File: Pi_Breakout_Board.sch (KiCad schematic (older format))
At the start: 74 parts, among them J1 Raspberry_Pi_2_3, J2 Conn_02x04_Odd_Even heater he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, J3 Conn_02x08_Odd_Even thermisto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, J4 Screw_Terminal_01x02, J5 Conn_01x08_Male, J6 Conn_01x08_Male, J7 Conn_01x02_Female, J8 Conn_01x03_Male, Q1 Q_NMOS_GDSD, Q2 Q_NMOS_GDSD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

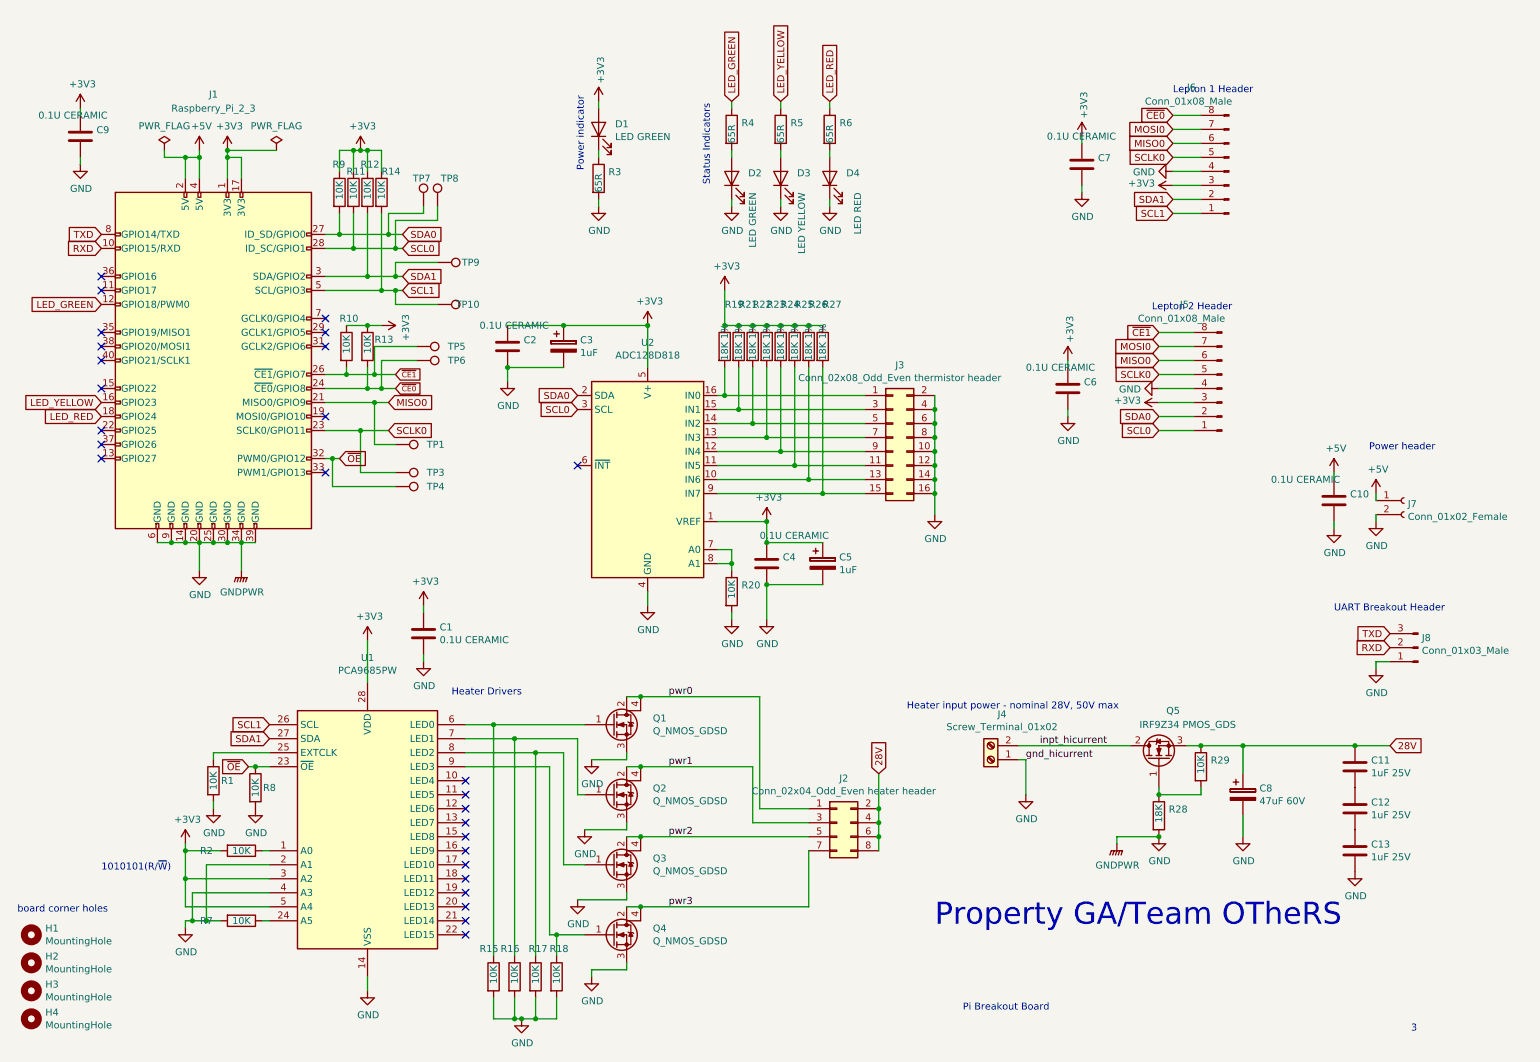
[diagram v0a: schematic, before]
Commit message: Routing updates + double checks. Silkscreen
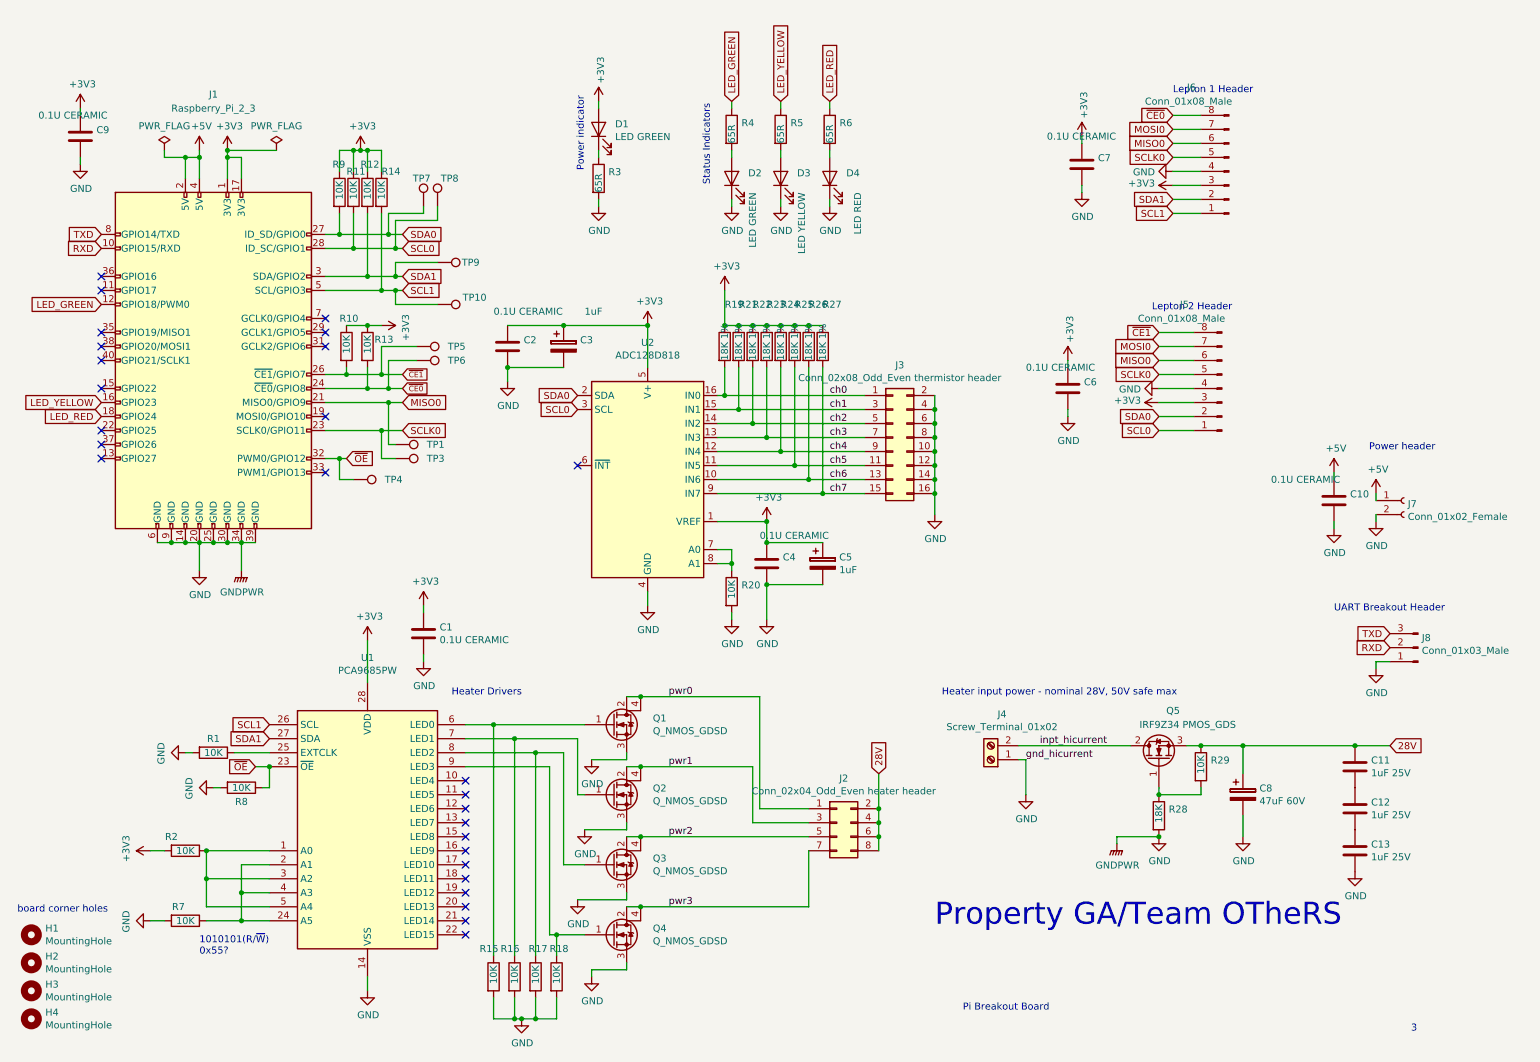
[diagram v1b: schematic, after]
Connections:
- net +3V3: no longer U1.3 (A2), U1.5 (A4)
- net GND: no longer U1.2 (A1), U1.4 (A3)
- net at R7.1, U1.24 (A5): now also U1.2 (A1), U1.4 (A3)
- net at R2.1, U1.1 (A0): now also U1.3 (A2), U1.5 (A4)
- net ch6: now reaches J3.13 (Pin_13), R26.2, U2.10 (IN6)
- net ch5: now reaches J3.11 (Pin_11), R25.2, U2.11 (IN5)
- net ch4: now reaches J3.9 (Pin_9), R24.2, U2.12 (IN4)
- net ch3: now reaches J3.7 (Pin_7), R23.2, U2.13 (IN3)
- net ch2: now reaches J3.5 (Pin_5), R22.2, U2.14 (IN2)
- net ch1: now reaches J3.3 (Pin_3), R21.2, U2.15 (IN1)
- net ch0: now reaches J3.1 (Pin_1), R19.2, U2.16 (IN0)
- net ch7: now reaches J3.15 (Pin_15), R27.2, U2.9 (IN7)
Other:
- note added: "1010101(R/~W)\n0x55?"
- note added: "Heater input power - nominal 28V, 50V safe max"
- note removed: "1010101(R/~W)"
- note removed: "Heater input power - nominal 28V, 50V max"
- moved on the sheet: R1, R2, R7, R8, TP3, TP4

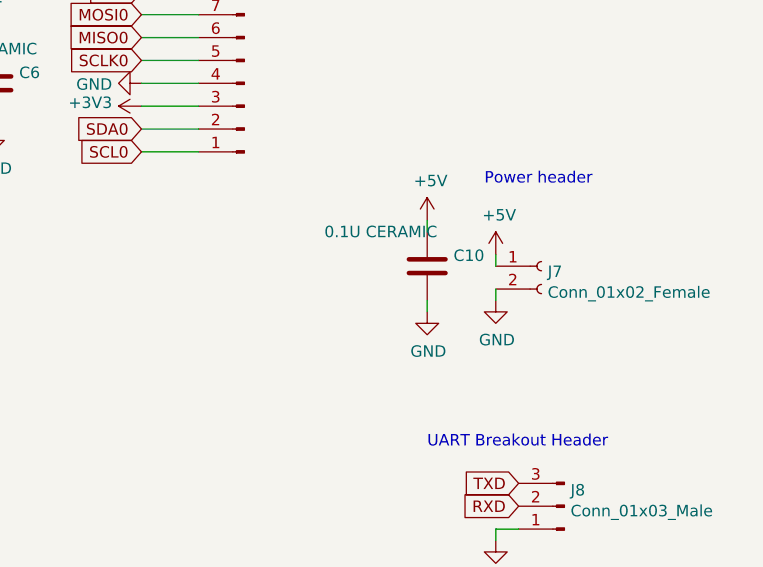
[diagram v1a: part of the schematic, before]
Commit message: add TVS diode
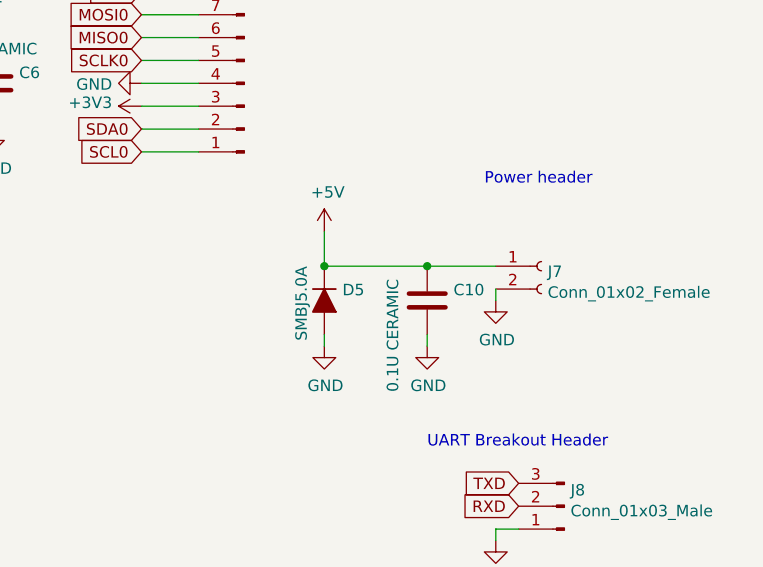
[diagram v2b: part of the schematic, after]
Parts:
- added D5: SMBJ5.0A, footprints:SMBJ5.0A, symbol Device:D_ALT
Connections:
- net +5V: now also D5.1 (K)
- net GND: now also D5.2 (A)
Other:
- moved on the sheet: C10
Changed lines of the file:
@@
 Wire Wire Line
 	10350 5000 10450 5000
-$Comp
-L power:+5V #PWR046
-U 1 1 5C584F51
-P 10350 3800
-F 0 "#PWR046" H 10350 3650 50  0001 C CNN
-F 1 "+5V" H 10365 3973 50  0000 C CNN
-F 2 "" H 10350 3800 50  0001 C CNN
-F 3 "" H 10350 3800 50  0001 C CNN
-	1    10350 3800
-	1    0    0    -1
-$EndComp
 Text GLabel 10450 4800 0    50   Input ~ 0
 TXD
@@
 L Device:C C10
 U 1 1 5C6E7D8F
-P 10050 3850
-F 0 "C10" H 10165 3896 50  0000 L CNN
-F 1 "0.1U CERAMIC" H 9600 4000 50  0000 L CNN
-F 2 "Capacitor_SMD:C_1210_3225Metric_Pad1.42x2.65mm_HandSolder" H 10088 3700 50  0001 C CNN
-F 3 "~" H 10050 3850 50  0001 C CNN
-	1    10050 3850
-	1    0    0    -1
-$EndComp
-Wire Wire Line
-	10050 3650 10050 3700
+P 10050 4000
+F 0 "C10" H 10165 4046 50  0000 L CNN
+F 1 "0.1U CERAMIC" V 9900 3600 50  0000 L CNN
+F 2 "Capacitor_SMD:C_1210_3225Metric_Pad1.42x2.65mm_HandSolder" H 10088 3850 50  0001 C CNN
+F 3 "~" H 10050 4000 50  0001 C CNN
+	1    10050 4000
+	1    0    0    -1
+$EndComp
 $Comp
 L power:GND #PWR043
 U 1 1 5C6E7D9D
-P 10050 4050
-F 0 "#PWR043" H 10050 3800 50  0001 C CNN
-F 1 "GND" H 10055 3877 50  0000 C CNN
-F 2 "" H 10050 4050 50  0001 C CNN
-F 3 "" H 10050 4050 50  0001 C CNN
-	1    10050 4050
-	1    0    0    -1
-$EndComp
-Wire Wire Line
-	10050 4000 10050 4050
+P 10050 4200
+F 0 "#PWR043" H 10050 3950 50  0001 C CNN
+F 1 "GND" H 10055 4027 50  0000 C CNN
+F 2 "" H 10050 4200 50  0001 C CNN
+F 3 "" H 10050 4200 50  0001 C CNN
+	1    10050 4200
+	1    0    0    -1
+$EndComp
+Wire Wire Line
+	10050 4150 10050 4200
 $Comp
 L power:+5V #PWR042
 U 1 1 5C6EFB3B
-P 10050 3650
-F 0 "#PWR042" H 10050 3500 50  0001 C CNN
-F 1 "+5V" H 10065 3823 50  0000 C CNN
-F 2 "" H 10050 3650 50  0001 C CNN
-F 3 "" H 10050 3650 50  0001 C CNN
-	1    10050 3650
+P 9600 3700
+F 0 "#PWR042" H 9600 3550 50  0001 C CNN
+F 1 "+5V" H 9615 3873 50  0000 C CNN
+F 2 "" H 9600 3700 50  0001 C CNN
+F 3 "" H 9600 3700 50  0001 C CNN
+	1    9600 3700
 	1    0    0    -1
 $EndComp
@@
 	1    0    0    -1
 $EndComp
-Wire Wire Line
-	10350 3800 10350 3850
 $Comp
 L power:GND #PWR0101
@@
 Text Label 6450 3800 0    50   ~ 0
 ch7
+Wire Wire Line
+	10350 3850 10050 3850
+$Comp
+L Device:D_ALT D5
+U 1 1 5C9D2EAA
+P 9600 4000
+F 0 "D5" V 9554 4079 50  0000 L CNN
+F 1 "SMBJ5.0A" H 9450 3900 50  0000 L CNN
+F 2 "footprints:SMBJ5.0A" H 9600 4000 50  0001 C CNN
+F 3 "~" H 9600 4000 50  0001 C CNN
+	1    9600 4000
+	0    1    1    0
+$EndComp
+$Comp
+L power:GND #PWR044
+U 1 1 5C9D2FB4
+P 9600 4200
+F 0 "#PWR044" H 9600 3950 50  0001 C CNN
+F 1 "GND" H 9605 4027 50  0000 C CNN
+F 2 "" H 9600 4200 50  0001 C CNN
+F 3 "" H 9600 4200 50  0001 C CNN
+	1    9600 4200
+	1    0    0    -1
+$EndComp
+Wire Wire Line
+	9600 4150 9600 4200
+Wire Wire Line
+	9600 3850 10050 3850
+Connection ~ 10050 3850
+Wire Wire Line
+	9600 3700 9600 3850
+Connection ~ 9600 3850
 $EndSCHEMATC

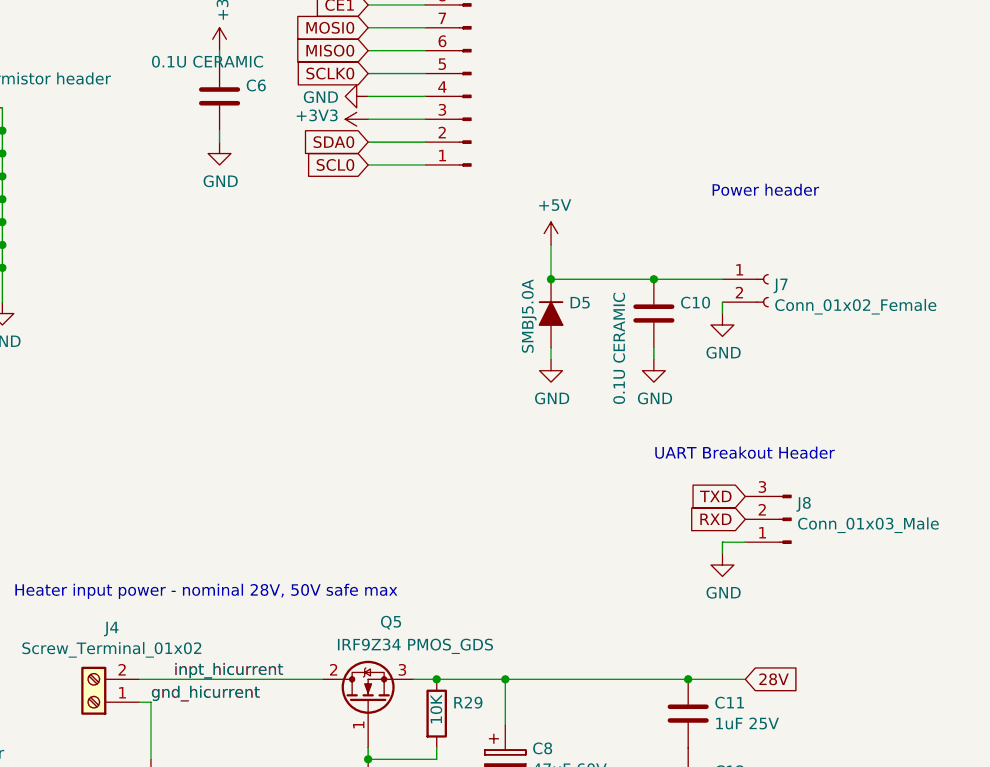
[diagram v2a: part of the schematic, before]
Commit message: Add 3V VCC pin to UART header (oops, shoulda had that). Other misc routing changes
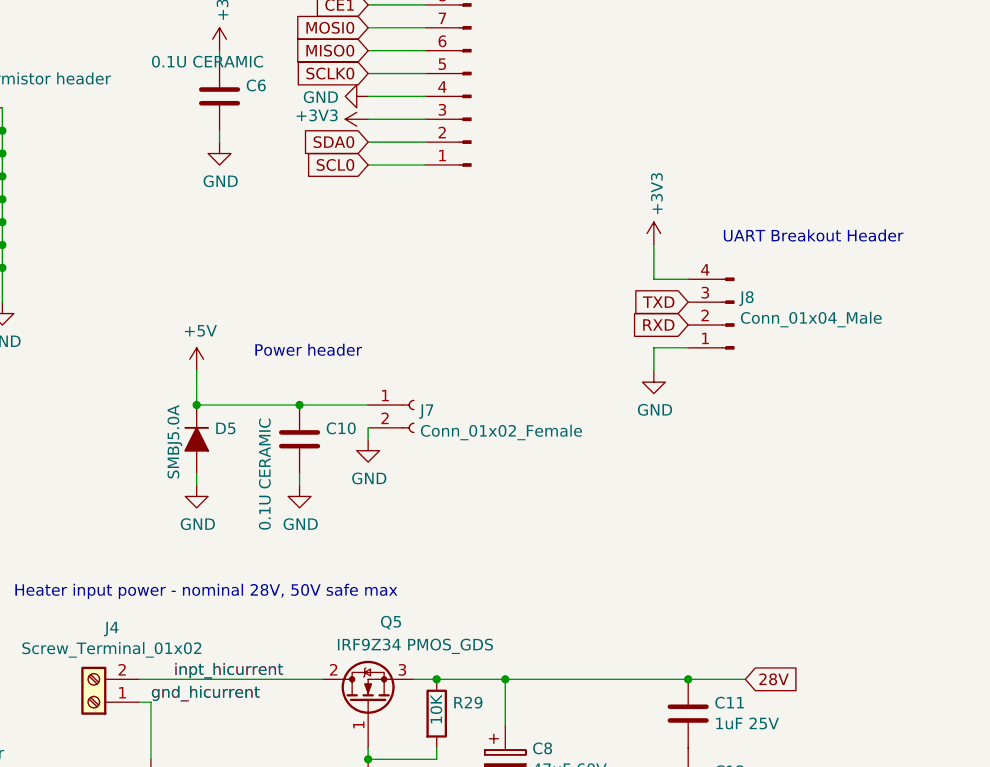
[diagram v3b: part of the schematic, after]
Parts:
- removed J8: Conn_01x03_Male, Connector_PinHeader_2.54mm:PinHeader_1x03_P2.54mm_Vertical, symbol Connector:Conn_01x03_Male
- added J8: Conn_01x04_Male, Connector_PinSocket_2.54mm:PinSocket_1x04_P2.54mm_Vertical, symbol Connector:Conn_01x04_Male
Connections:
- net +3V3: now also J8.4 (Pin_4)
- net GND: now also J8.1 (Pin_1)
- net RXD: now also J8.2 (Pin_2)
- net TXD: now also J8.3 (Pin_3)
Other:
- moved on the sheet: C10, D5, J7
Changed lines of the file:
@@
 L power:GND #PWR047
 U 1 1 5C583A1E
-P 10350 5050
-F 0 "#PWR047" H 10350 4800 50  0001 C CNN
-F 1 "GND" H 10355 4877 50  0000 C CNN
-F 2 "" H 10350 5050 50  0001 C CNN
-F 3 "" H 10350 5050 50  0001 C CNN
-	1    10350 5050
-	1    0    0    -1
-$EndComp
-Wire Wire Line
-	10350 5050 10350 5000
-Wire Wire Line
-	10350 5000 10450 5000
-Text GLabel 10450 4800 0    50   Input ~ 0
+P 10050 4250
+F 0 "#PWR047" H 10050 4000 50  0001 C CNN
+F 1 "GND" H 10055 4077 50  0000 C CNN
+F 2 "" H 10050 4250 50  0001 C CNN
+F 3 "" H 10050 4250 50  0001 C CNN
+	1    10050 4250
+	1    0    0    -1
+$EndComp
+Wire Wire Line
+	10050 4250 10050 4150
+Wire Wire Line
+	10050 4150 10200 4150
+Text GLabel 10200 3950 0    50   Input ~ 0
 TXD
-Text GLabel 10450 4900 0    50   Input ~ 0
+Text GLabel 10200 4050 0    50   Input ~ 0
 RXD
-Text Notes 10050 4650 0    50   ~ 0
+Text Notes 10350 3700 0    50   ~ 0
 UART Breakout Header
 Text Notes 7250 5250 0    50   ~ 0
@@
 L Device:C C10
 U 1 1 5C6E7D8F
-P 10050 4000
-F 0 "C10" H 10165 4046 50  0000 L CNN
-F 1 "0.1U CERAMIC" V 9900 3600 50  0000 L CNN
-F 2 "Capacitor_SMD:C_1210_3225Metric_Pad1.42x2.65mm_HandSolder" H 10088 3850 50  0001 C CNN
-F 3 "~" H 10050 4000 50  0001 C CNN
-	1    10050 4000
+P 8500 4550
+F 0 "C10" H 8615 4596 50  0000 L CNN
+F 1 "0.1U CERAMIC" V 8350 4150 50  0000 L CNN
+F 2 "Capacitor_SMD:C_1210_3225Metric_Pad1.42x2.65mm_HandSolder" H 8538 4400 50  0001 C CNN
+F 3 "~" H 8500 4550 50  0001 C CNN
+	1    8500 4550
 	1    0    0    -1
 $EndComp
@@
 L power:GND #PWR043
 U 1 1 5C6E7D9D
-P 10050 4200
-F 0 "#PWR043" H 10050 3950 50  0001 C CNN
-F 1 "GND" H 10055 4027 50  0000 C CNN
-F 2 "" H 10050 4200 50  0001 C CNN
-F 3 "" H 10050 4200 50  0001 C CNN
-	1    10050 4200
-	1    0    0    -1
-$EndComp
-Wire Wire Line
-	10050 4150 10050 4200
+P 8500 4750
+F 0 "#PWR043" H 8500 4500 50  0001 C CNN
+F 1 "GND" H 8505 4577 50  0000 C CNN
+F 2 "" H 8500 4750 50  0001 C CNN
+F 3 "" H 8500 4750 50  0001 C CNN
+	1    8500 4750
+	1    0    0    -1
+$EndComp
+Wire Wire Line
+	8500 4700 8500 4750
 $Comp
 L power:+5V #PWR042
 U 1 1 5C6EFB3B
-P 9600 3700
-F 0 "#PWR042" H 9600 3550 50  0001 C CNN
-F 1 "+5V" H 9615 3873 50  0000 C CNN
-F 2 "" H 9600 3700 50  0001 C CNN
-F 3 "" H 9600 3700 50  0001 C CNN
-	1    9600 3700
+P 8050 4250
+F 0 "#PWR042" H 8050 4100 50  0001 C CNN
+F 1 "+5V" H 8065 4423 50  0000 C CNN
+F 2 "" H 8050 4250 50  0001 C CNN
+F 3 "" H 8050 4250 50  0001 C CNN
+	1    8050 4250
 	1    0    0    -1
 $EndComp
@@
 L Connector:Conn_01x02_Female J7
 U 1 1 5C91FC8D
-P 10550 3850
-F 0 "J7" H 10577 3826 50  0000 L CNN
-F 1 "Conn_01x02_Female" H 10577 3735 50  0000 L CNN
-F 2 "Connector_PinSocket_2.54mm:PinSocket_1x02_P2.54mm_Horizontal" H 10550 3850 50  0001 C CNN
-F 3 "~" H 10550 3850 50  0001 C CNN
-	1    10550 3850
+P 9000 4400
+F 0 "J7" H 9027 4376 50  0000 L CNN
+F 1 "Conn_01x02_Female" H 9027 4285 50  0000 L CNN
+F 2 "Connector_PinSocket_2.54mm:PinSocket_1x02_P2.54mm_Horizontal" H 9000 4400 50  0001 C CNN
+F 3 "~" H 9000 4400 50  0001 C CNN
+	1    9000 4400
 	1    0    0    -1
 $EndComp
@@
 L power:GND #PWR0101
 U 1 1 5C9343D0
-P 10350 4000
-F 0 "#PWR0101" H 10350 3750 50  0001 C CNN
-F 1 "GND" H 10355 3827 50  0000 C CNN
-F 2 "" H 10350 4000 50  0001 C CNN
-F 3 "" H 10350 4000 50  0001 C CNN
-	1    10350 4000
-	1    0    0    -1
-$EndComp
-Wire Wire Line
-	10350 3950 10350 4000
-Text Notes 10300 3500 0    50   ~ 0
+P 8800 4550
+F 0 "#PWR0101" H 8800 4300 50  0001 C CNN
+F 1 "GND" H 8805 4377 50  0000 C CNN
+F 2 "" H 8800 4550 50  0001 C CNN
+F 3 "" H 8800 4550 50  0001 C CNN
+	1    8800 4550
+	1    0    0    -1
+$EndComp
+Wire Wire Line
+	8800 4500 8800 4550
+Text Notes 8300 4200 0    50   ~ 0
 Power header
-$Comp
-L Connector:Conn_01x03_Male J8
-U 1 1 5C9743D8
-P 10650 4900
-F 0 "J8" H 10623 4830 50  0000 R CNN
-F 1 "Conn_01x03_Male" H 10623 4921 50  0000 R CNN
-F 2 "Connector_PinHeader_2.54mm:PinHeader_1x03_P2.54mm_Vertical" H 10650 4900 50  0001 C CNN
-F 3 "~" H 10650 4900 50  0001 C CNN
-	1    10650 4900
-	-1   0    0    1
-$EndComp
 Text Notes 5600 1600 1    50   ~ 0
 Status Indicators
@@
 ch7
 Wire Wire Line
-	10350 3850 10050 3850
+	8800 4400 8500 4400
 $Comp
 L Device:D_ALT D5
 U 1 1 5C9D2EAA
-P 9600 4000
-F 0 "D5" V 9554 4079 50  0000 L CNN
-F 1 "SMBJ5.0A" H 9450 3900 50  0000 L CNN
-F 2 "footprints:SMBJ5.0A" H 9600 4000 50  0001 C CNN
-F 3 "~" H 9600 4000 50  0001 C CNN
-	1    9600 4000
+P 8050 4550
+F 0 "D5" V 8004 4629 50  0000 L CNN
+F 1 "SMBJ5.0A" H 7900 4450 50  0000 L CNN
+F 2 "footprints:SMBJ5.0A" H 8050 4550 50  0001 C CNN
+F 3 "~" H 8050 4550 50  0001 C CNN
+	1    8050 4550
 	0    1    1    0
 $EndComp
@@
 L power:GND #PWR044
 U 1 1 5C9D2FB4
-P 9600 4200
-F 0 "#PWR044" H 9600 3950 50  0001 C CNN
-F 1 "GND" H 9605 4027 50  0000 C CNN
-F 2 "" H 9600 4200 50  0001 C CNN
-F 3 "" H 9600 4200 50  0001 C CNN
-	1    9600 4200
-	1    0    0    -1
-$EndComp
-Wire Wire Line
-	9600 4150 9600 4200
-Wire Wire Line
-	9600 3850 10050 3850
-Connection ~ 10050 3850
-Wire Wire Line
-	9600 3700 9600 3850
-Connection ~ 9600 3850
+P 8050 4750
+F 0 "#PWR044" H 8050 4500 50  0001 C CNN
+F 1 "GND" H 8055 4577 50  0000 C CNN
+F 2 "" H 8050 4750 50  0001 C CNN
+F 3 "" H 8050 4750 50  0001 C CNN
+	1    8050 4750
+	1    0    0    -1
+$EndComp
+Wire Wire Line
+	8050 4700 8050 4750
+Wire Wire Line
+	8050 4400 8500 4400
+Connection ~ 8500 4400
+Wire Wire Line
+	8050 4250 8050 4400
+Connection ~ 8050 4400
+$Comp
+L Connector:Conn_01x04_Male J8
+U 1 1 5CB3FDBF
+P 10400 4050
+F 0 "J8" H 10373 3930 50  0000 R CNN
+F 1 "Conn_01x04_Male" H 10373 4021 50  0000 R CNN
+F 2 "Connector_PinSocket_2.54mm:PinSocket_1x04_P2.54mm_Vertical" H 10400 4050 50  0001 C CNN
+F 3 "~" H 10400 4050 50  0001 C CNN
+	1    10400 4050
+	-1   0    0    1
+$EndComp
+$Comp
+L power:+3V3 #PWR046
+U 1 1 5CB69318
+P 10050 3700
+F 0 "#PWR046" H 10050 3550 50  0001 C CNN
+F 1 "+3V3" V 10065 3828 50  0000 L CNN
+F 2 "" H 10050 3700 50  0001 C CNN
+F 3 "" H 10050 3700 50  0001 C CNN
+	1    10050 3700
+	1    0    0    -1
+$EndComp
+Wire Wire Line
+	10050 3700 10050 3850
+Wire Wire Line
+	10050 3850 10200 3850
 $EndSCHEMATC
